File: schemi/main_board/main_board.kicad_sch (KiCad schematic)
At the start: 44 parts, among them J1 PICKIT, J2 FC1, J3 FC2, J4 ACQUA, J5 Conn, J6 FINESTRE, K1 Fujitsu_FTR-LYAA005x, K2 Fujitsu_FTR-LYAA005x, Q1 2N2222A, Q2 2N2222A, SW1 START, SW2 STOP, SW3 MODO, U1 D168K, U1 PIC16F887-IP, U2 D168K

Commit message: update main board
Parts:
- removed J4: ACQUA, symbol Connector:Screw_Terminal_01x02
- removed J6: FINESTRE, symbol Connector:Screw_Terminal_01x02
- removed K1, K2: Fujitsu_FTR-LYAA005x, Relay_THT:Relay_SPST-NO_Fujitsu_FTR-LYAA005x_FormA_Vertical, symbol Relay:Fujitsu_FTR-LYAA005x
- removed SW3: MODO, Button_Switch_SMD:Nidec_Copal_CAS-120A, symbol Switch:SW_Nidec_CAS-120A1
- removed U1, U2: D168K, Display_7Segment:D1X8K, symbol Display_Character:D168K
- added C2: 220nF, Capacitor_THT:C_Disc_D4.7mm_W2.5mm_P5.00mm, symbol Device:C
- added C4, C5: 100nF, Capacitor_THT:C_Disc_D4.7mm_W2.5mm_P5.00mm, symbol Device:C
- added C6: 4.7m, Capacitor_THT:CP_Radial_D12.5mm_P5.00mm, symbol Device:C
- added D10, D11, D12: LED, LED_THT:LED_D5.0mm, symbol Device:LED
- added D7: 1N4004, Diode_THT:D_DO-41_SOD81_P10.16mm_Horizontal, symbol Diode:1N4004
- added D8: 1N4007, Diode_THT:D_DO-41_SOD81_P10.16mm_Horizontal, symbol Diode:1N4007
- added H1, H2, H3, H4: MountingHole_Pad, MountingHole:MountingHole_2.5mm_Pad, symbol Mechanical:MountingHole_Pad
- added J4: Conn_Relè, TerminalBlock:TerminalBlock_MaiXu_MX126-5.0-06P_1x06_P5.00mm, symbol Connector:Screw_Terminal_01x06
- added J6: Power_barrel, Connector_BarrelJack:BarrelJack_GCT_DCJ200-10-A_Horizontal, symbol Connector:Barrel_Jack_MountingPin
- added J7: sensore_temp, Connector_PinHeader_2.54mm:PinHeader_1x03_P2.54mm_Horizontal, symbol Connector_Generic:Conn_01x03
- added J8: Power, TerminalBlock:TerminalBlock_MaiXu_MX126-5.0-02P_1x02_P5.00mm, symbol Connector:Screw_Terminal_01x02
- added J9: controllo_alimentazione, Connector_PinSocket_2.54mm:PinSocket_1x03_P2.54mm_Vertical, symbol Connector:Conn_01x03_Socket
- added K1: Ventilazione, Relay_THT:Relay_SPDT_Finder_40.41, symbol Relay:FINDER-40.41
- added K2: finestre, Relay_THT:Relay_SPDT_Finder_40.41, symbol Relay:FINDER-40.41
- added K3: acqua, Relay_THT:Relay_SPDT_Finder_40.41, symbol Relay:FINDER-40.41
- added Q3, Q4, Q5: 2N2222A, Package_TO_SOT_THT:TO-92_Inline_Wide, symbol Simulation_SPICE:NPN
- added R11, R31, R32, R8, R9: R, Resistor_THT:R_Axial_DIN0207_L6.3mm_D2.5mm_P10.16mm_Horizontal, symbol Device:R
- added R30: 1K, Resistor_THT:R_Axial_DIN0207_L6.3mm_D2.5mm_P10.16mm_Horizontal, symbol Device:R
- added SW3: MODO, Connector_PinHeader_2.54mm:PinHeader_1x02_P2.54mm_Vertical, symbol Switch:SW_SPST
- added U4: LM7805_TO220, Package_TO_SOT_THT:TO-220-3_Vertical, symbol Regulator_Linear:LM7805_TO220
- added U5, U6: SM420561N, Display_7Segment:7SegmentLED_LTS6760_LTS6780, symbol Display_Character:SM420561N
- D3, D4, D5, D6: footprint (none) -> LED_THT:LED_D5.0mm
- J1: footprint Connector_PinSocket_2.54mm:PinSocket_1x06_P2.54mm_Vertical -> Connector_PinHeader_2.54mm:PinHeader_1x06_P2.54mm_Horizontal
- J2, J3: footprint (none) -> Connector_PinHeader_2.54mm:PinHeader_1x02_P2.54mm_Horizontal
- J5: value Conn -> MOTORE; footprint Connector_PinSocket_2.54mm:PinSocket_1x05_P2.54mm_Vertical -> Connector_PinHeader_2.54mm:PinHeader_1x05_P2.54mm_Horizontal
- Q1, Q2: footprint (none) -> Package_TO_SOT_THT:TO-92_Inline_Wide
- R1, R15, R16, R17, R19, R2, R20, R21, R22, R23, R24, R25, R26, R27, R28, R29, R3, R4, R5, R6, R7: footprint (none) -> Resistor_THT:R_Axial_DIN0207_L6.3mm_D2.5mm_P10.16mm_Horizontal
- SW1, SW2: footprint (none) -> Connector_PinHeader_2.54mm:PinHeader_1x02_P2.54mm_Vertical
- U1: footprint (none) -> Package_DIP:DIP-40_W15.24mm_LongPads
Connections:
- net D1A is gone; now on net DA: R1.1
- net D1B is gone; now on net DB: R2.1
- net D1C is gone; now on net DC: R3.1
- net D1D is gone; now on net DD: R4.1
- net D1E is gone; now on net DE: R5.1
- net +12V: now also C2.1, C6.1, D7.1 (K), D8.1 (K), J9.3 (Pin_3), K1.A1, K2.A1, K3.A1, R31.1, R32.1, U4.1 (VI)
- net +5V: now also C4.1, C5.1, J7.3 (Pin_3), J9.1 (Pin_1), R11.1, U4.3 (VO)
- net ACQUA: now also U1.17 (P1A/CCP1/RC2)
- net Direzione: now also U1.6 (C1OUT/T0CKI/RA4)
- net Encoder A: now also U1.16 (T1OSI/CCP2/RC1)
- net FC1: now also U1.3 (C12IN1-/AN1/RA1)
- net FC2: now also U1.2 (C12IN0-/ULPWU/AN0/RA0)
- net FINESTRE: now also U1.18 (SCL/SCK/RC3)
- net GND: now also C2.2, C4.2, C5.2, C6.2, D10.1 (K), H1.1, H2.1, H3.1, H4.1, J6.2, J6.MP (MountPin), J7.1 (Pin_1), J8.2 (Pin_2), J9.2 (Pin_2), Q3.3 (E), Q4.3 (E), Q5.3 (E), SW3.2 (B), U4.2 (GND)
- net MODO: now also U1.21 (RD2), SW3.1 (A)
- net Power: now also U1.5 (C1IN+/Vref+/AN3/RA3)
- net START: now also U1.22 (RD3)
- net STOP: now also U1.27 (RD4)
- net Velocità: now also U1.7 (C2OUT/~{SS}/AN4/RA5)
- net at D1.2 (A), D6.1 (K), Q1.1 (C): now also K3.A2
- net at R6.2: now also U5.9 (F), U6.9 (F)
- net at R1.2: now also U5.7 (A), U6.7 (A)
- net at R5.2: now also U5.1 (E), U6.1 (E)
- net at R7.2: now also U5.10 (G), U6.10 (G)
- net at R4.2: now also U5.2 (D), U6.2 (D)
- net at R3.2: now also U5.4 (C), U6.4 (C)
- net at R2.2: now also U5.6 (B), U6.6 (B)
- net at D2.2 (A), Q2.1 (C): now also D11.1 (K), K2.A2
- net VENTILAZIONE: now reaches U1.15 (T10S0/T1CKI/RC0)
- net VENTILAZIONE: now also R30.1
- net EN_D1: now reaches U1.29 (RD6/P1C)
- net EN_D1: now also R8.2
- net EN_D2: now reaches U1.30 (RD7/P1D)
- net EN_D2: now also R9.2
- net DA: now reaches U1.34 (C12IN3-/AN10/RB1)
- net DB: now reaches U1.35 (AN8/RB2)
- net DC: now reaches U1.36 (C12IN2-/PGM/AN9/RB3)
- net DD: now reaches U1.37 (AN11/RB4)
- net DE: now reaches U1.38 (~{T1G}/AN13/RB5)
- net TEMP: now reaches U1.4 (C2IN+/CVref/Vref-/AN2/RA2)
- net TEMP: now also J7.2 (Pin_2)
- net D1F renamed DF
- net DF: now also J1.5 (Pin_5), U1.39 (ICSPCLK/RB6)
- net D1G renamed DG
- net DG: now also J1.4 (Pin_4), U1.40 (ICSPDAT/RB7)
- net Encoder B: no longer names the net of J5.4 (Pin_4)
- removed net ICSPCLK: J1.4 (Pin_4), U1.39 (ICSPCLK/RB6)
- removed net ICSPDAT: J1.5 (Pin_5), U1.40 (ICSPDAT/RB7)
- new net: Q3.2 (B), R8.1
- new net: D12.1 (K), D7.2 (A), K1.A2, Q5.1 (C)
- new net: D12.2 (A), R32.2
- new net: Q4.1 (C), U6.3 (CC), U6.8 (CC)
- new net: Q5.2 (B), R30.2
- new net: D8.2 (A), J6.1, J8.1 (Pin_1)
- new net: Q4.2 (B), R9.1
- new net: D11.2 (A), R31.2
- new net: Q3.1 (C), U5.3 (CC), U5.8 (CC)
- new net: D10.2 (A), R11.2
- new net R1A: J4.1 (Pin_1), K1.14
- new net R1B: J4.2 (Pin_2), K1.11
- new net R2A: J4.3 (Pin_3), K2.14
- new net R2B: J4.4 (Pin_4), K2.11
- new net R3A: J4.5 (Pin_5), K3.14
- new net R3B: J4.6 (Pin_6), K3.11
- no-connect marks 2 -> 20
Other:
- note added: "ALIMENTAZIONE"
- note added: "CONN RELÉ"
- note added: "DISPLAY 7 SEGMENTI 2 DIGIT"
- note added: "FINESTRE"
- note added: "FORI DI MONTAGGIO"
- note added: "IN"
- note added: "MORSETTO DI ALIMENTAZIONE"
- note added: "OUT"
- note added: "PIC16F887"
- note added: "REGOLATORE"
- note added: "SISTEMA DI VENTILAZIONE"
- note added: "TEMPERATURA"
- note removed: "VENTILAZIONE - FINESTRE"
- moved on the sheet: D1, D2, D3, D4, D5, D6, J1, J2, J3, J5, Q1, Q2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

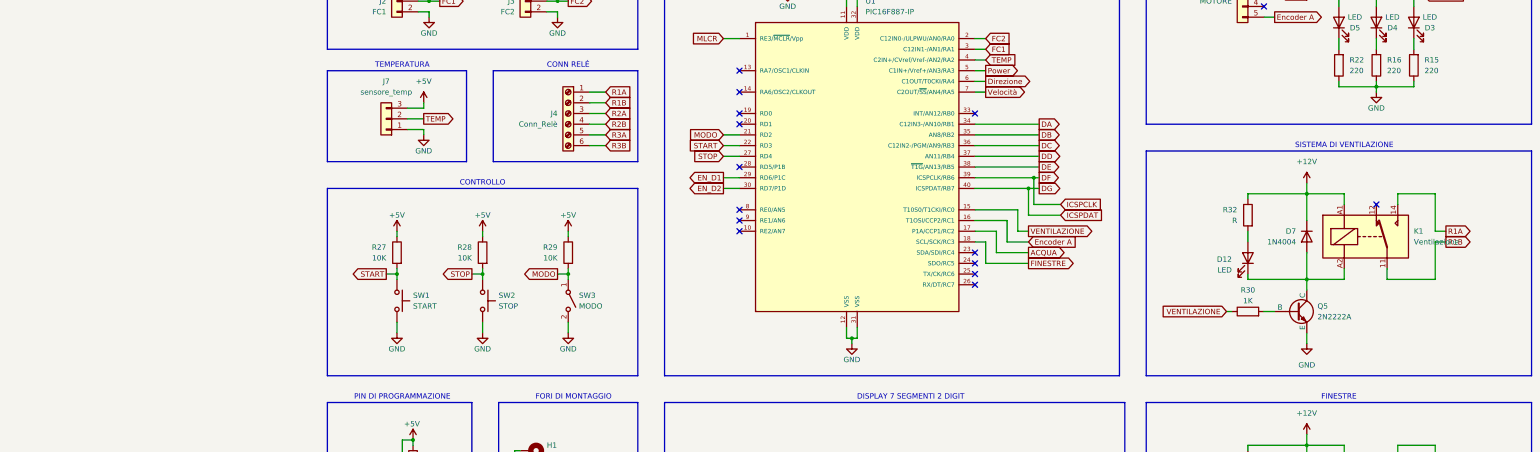
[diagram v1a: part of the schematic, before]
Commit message: aggiunto la visualizzazione al panello di controllo
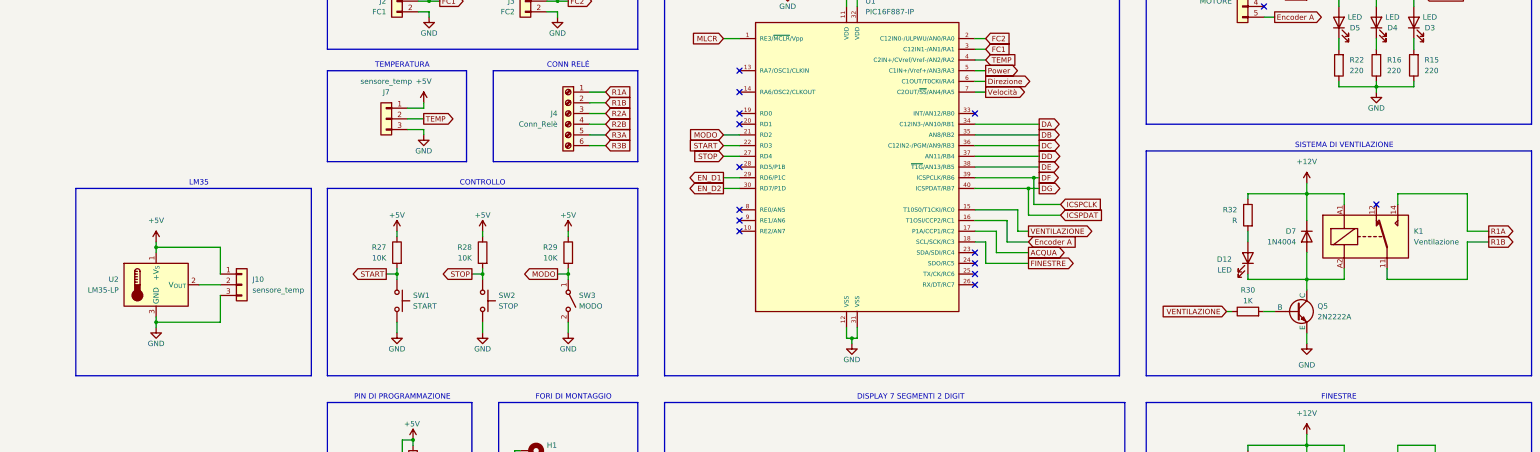
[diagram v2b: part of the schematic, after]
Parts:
- added J10: sensore_temp, Connector_PinHeader_2.54mm:PinHeader_1x03_P2.54mm_Horizontal, symbol Connector_Generic:Conn_01x03
- added U2: LM35-LP, Package_TO_SOT_THT:TO-92_Inline, symbol Sensor_Temperature:LM35-LP
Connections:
- net +5V: now also J7.1 (Pin_1), J10.1 (Pin_1), U2.1 (+V_{S}); no longer J7.3 (Pin_3)
- net GND: now also J7.3 (Pin_3), J10.3 (Pin_3), U2.3 (GND); no longer J7.1 (Pin_1)
- new net: J10.2 (Pin_2), U2.2 (V_{OUT})
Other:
- note added: "LM35"
- moved on the sheet: J7
